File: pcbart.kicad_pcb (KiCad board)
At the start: 2 copper layers, 150.7 x 25 mm, 4 parts

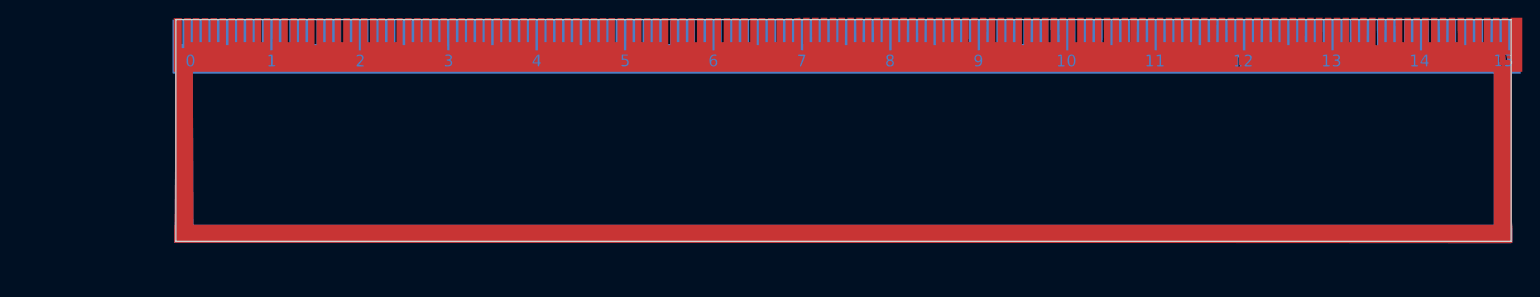
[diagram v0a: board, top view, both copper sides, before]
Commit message: Extend ruler,  use rounded edges, sort out numbers
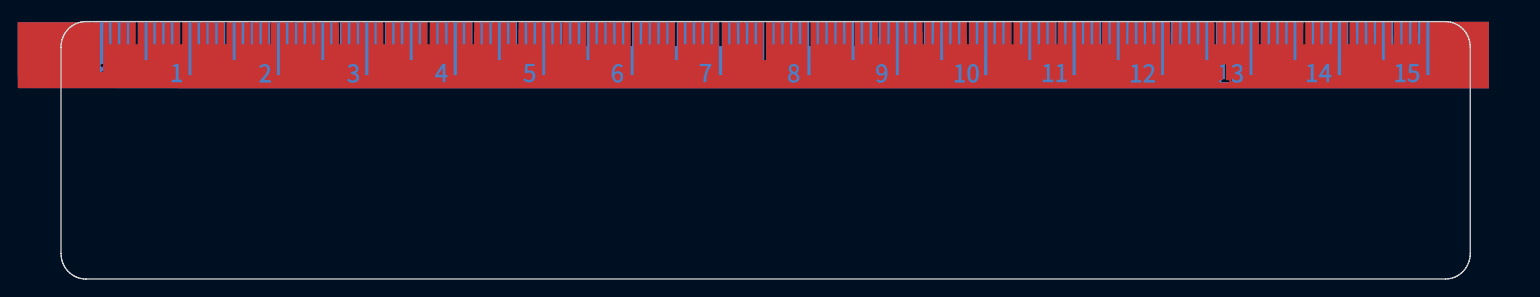
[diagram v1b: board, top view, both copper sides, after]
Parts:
- removed the G*** at (0.00, 0.00) (x4)
- added G*** (x4): LOGO, LOGO, F.Cu at (0.00, 0.00)
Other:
- board size 150.7 x 25 mm -> 159.1 x 29.1 mm
